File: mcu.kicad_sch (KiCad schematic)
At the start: 7 parts, among them SW1 SW_MEC_5E, U9 ESP32-S3-WROOM-1-N16R8

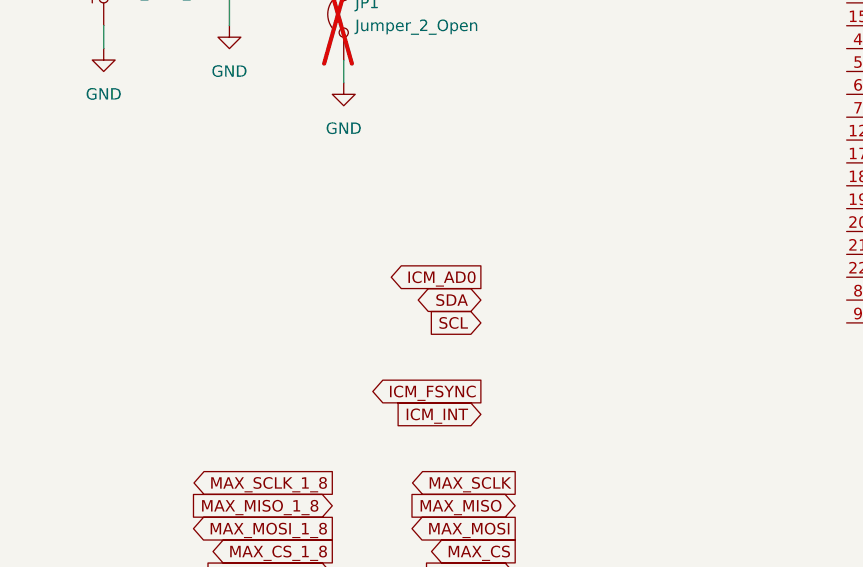
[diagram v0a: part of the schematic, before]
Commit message: Add power rail
Battery charger
3.3V LDO
1.8V LDO
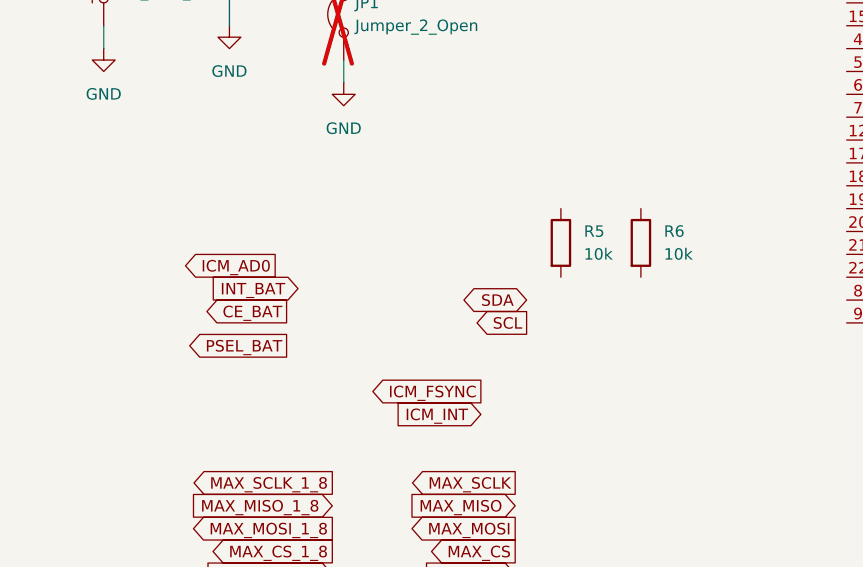
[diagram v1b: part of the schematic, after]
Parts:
- added R5, R6: 10k, symbol Device:R
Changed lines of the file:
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@@
+		)
+	)
+	(global_label "PSEL_BAT"
+		(shape output)
+		(at 77.47 120.65 180)
+		(fields_autoplaced yes)
+		(effects
+			(font
+				(size 1.27 1.27)
+			)
+			(justify right)
+		)
+		(property "Intersheetrefs" "${INTERSHEET_REFS}"
+			(at 65.5344 120.65 0)
+			(effects
+				(font
+					(size 1.27 1.27)
+				)
+				(justify right)
+				(hide yes)
+			)
 		)
 	)
 	(global_label "ICM_AD0"
 		(shape output)
-		(at 99.06 113.03 180)
-		(fields_autoplaced yes)
-		(effects
-			(font
-				(size 1.27 1.27)
-			)
-			(justify right)
-		)
-		(property "Intersheetrefs" "${INTERSHEET_REFS}"
-			(at 88.2129 113.03 0)
+		(at 76.2 111.76 180)
+		(fields_autoplaced yes)
+		(effects
+			(font
+				(size 1.27 1.27)
+			)
+			(justify right)
+		)
+		(property "Intersheetrefs" "${INTERSHEET_REFS}"
+			(at 65.3529 111.76 0)
 			(effects
 				(font
@@
 		)
 	)
+	(global_label "INT_BAT"
+		(shape input)
+		(at 78.74 114.3 180)
+		(fields_autoplaced yes)
+		(effects
+			(font
+				(size 1.27 1.27)
+			)
+			(justify right)
+		)
+		(property "Intersheetrefs" "${INTERSHEET_REFS}"
+			(at 68.5581 114.3 0)
+			(effects
+				(font
+					(size 1.27 1.27)
+				)
+				(justify right)
+				(hide yes)
+			)
+		)
+	)
 	(global_label "D-"
 		(shape bidirectional)
@@
 		)
 	)
+	(global_label "CE_BAT"
+		(shape output)
+		(at 77.47 116.84 180)
+		(fields_autoplaced yes)
+		(effects
+			(font
+				(size 1.27 1.27)
+			)
+			(justify right)
+		)
+		(property "Intersheetrefs" "${INTERSHEET_REFS}"
+			(at 67.772 116.84 0)
+			(effects
+				(font
+					(size 1.27 1.27)
+				)
+				(justify right)
+				(hide yes)
+			)
+		)
+	)
 	(global_label "MAX_INT_1_8"
 		(shape input)
@@
 	)
 	(global_label "SCL"
-		(shape input)
-		(at 99.06 118.11 180)
-		(fields_autoplaced yes)
-		(effects
-			(font
-				(size 1.27 1.27)
-			)
-			(justify right)
-		)
-		(property "Intersheetrefs" "${INTERSHEET_REFS}"
-			(at 92.5672 118.11 0)
+		(shape output)
+		(at 104.14 118.11 180)
+		(fields_autoplaced yes)
+		(effects
+			(font
+				(size 1.27 1.27)
+			)
+			(justify right)
+		)
+		(property "Intersheetrefs" "${INTERSHEET_REFS}"
+			(at 97.6472 118.11 0)
 			(effects
 				(font
@@
 	(global_label "SDA"
 		(shape bidirectional)
-		(at 99.06 115.57 180)
-		(fields_autoplaced yes)
-		(effects
-			(font
-				(size 1.27 1.27)
-			)
-			(justify right)
-		)
-		(property "Intersheetrefs" "${INTERSHEET_REFS}"
-			(at 91.3954 115.57 0)
+		(at 104.14 115.57 180)
+		(fields_autoplaced yes)
+		(effects
+			(font
+				(size 1.27 1.27)
+			)
+			(justify right)
+		)
+		(property "Intersheetrefs" "${INTERSHEET_REFS}"
+			(at 96.4754 115.57 0)
 			(effects
 				(font
@@
 	)
 	(symbol
+		(lib_id "Device:R")
+		(at 116.84 109.22 0)
+		(unit 1)
+		(exclude_from_sim no)
+		(in_bom yes)
+		(on_board yes)
+		(dnp no)
+		(fields_autoplaced yes)
+		(property "Reference" "R6"
+			(at 119.38 107.9499 0)
+			(effects
+				(font
+					(size 1.27 1.27)
+				)
+				(justify left)
+			)
+		)
+		(property "Value" "10k"
+			(at 119.38 110.4899 0)
+			(effects
+				(font
+					(size 1.27 1.27)
+				)
+				(justify left)
+			)
+		)
+		(property "Footprint" ""
+			(at 115.062 109.22 90)
+			(effects
+				(font
+					(size 1.27 1.27)
+				)
+				(hide yes)
+			)
+		)
+		(property "Datasheet" "~"
+			(at 116.84 109.22 0)
+			(effects
+				(font
+					(size 1.27 1.27)
+				)
+				(hide yes)
+			)
+		)
+		(property "Description" "Resistor"
+			(at 116.84 109.22 0)
+			(effects
+				(font
+					(size 1.27 1.27)
+				)
+				(hide yes)
+			)
+		)
+		(pin "2"
+		)
+		(pin "1"
+		)
+		(instances
+			(project "horsesense"
+				(path "/f18e9cf6-8519-4493-9888-bebeac60f18c/4f5da0f7-32d4-4c35-9e09-eaff048f43d5"
+					(reference "R6")
+					(unit 1)
+				)
+			)
+		)
+	)
+	(symbol
 		(lib_id "power:GND")
 		(at 154.94 127 0)
@@
 					(unit 1)
 				)
+			)
+		)
+	)
+	(symbol
+		(lib_id "Device:R")
+		(at 107.95 109.22 0)
+		(unit 1)
+		(exclude_from_sim no)
+		(in_bom yes)
+		(on_board yes)
+		(dnp no)
+		(fields_autoplaced yes)
+		(property "Reference" "R5"
+			(at 110.49 107.9499 0)
+			(effects
+				(font
+					(size 1.27 1.27)
+				)
+				(justify left)
+			)
+		)
+		(property "Value" "10k"
+			(at 110.49 110.4899 0)
+			(effects
+				(font
+					(size 1.27 1.27)
+				)
+				(justify left)
+			)
+		)
+		(property "Footprint" ""
+			(at 106.172 109.22 90)
+			(effects
+				(font
+					(size 1.27 1.27)
+				)
+				(hide yes)
+			)
+		)
+		(property "Datasheet" "~"
+			(at 107.95 109.22 0)
+			(effects
+				(font
+					(size 1.27 1.27)
+				)
+				(hide yes)
+			)
+		)
+		(property "Description" "Resistor"
+			(at 107.95 109.22 0)
+			(effects
+				(font
+					(size 1.27 1.27)
+				)
+				(hide yes)
+			)
+		)
+		(pin "2"
+		)
+		(pin "1"
+		)
+		(instances
+			(project "horsesense"
+				(path "/f18e9cf6-8519-4493-9888-bebeac60f18c/4f5da0f7-32d4-4c35-9e09-eaff048f43d5"
+					(reference "R5")
+					(unit 1)
+				)

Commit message: Routage complet
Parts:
- removed JP1: Jumper_2_Open, Connector_PinHeader_2.54mm:PinHeader_1x02_P2.54mm_Vertical, symbol Jumper:Jumper_2_Open
- added C3, C32: 100n, Capacitor_SMD:C_0805_2012Metric, symbol Device:C
- added J4: Conn_01x04, Connector_PinHeader_1.27mm:PinHeader_1x04_P1.27mm_Vertical, symbol Connector_Generic:Conn_01x04
- added SW2: EVQ-P7A01P, Button_Switch_SMD:SW_SPST_EVQP7A, symbol Switch:SW_Omron_B3FS
- added U2: TXB0304RUT, Package_DFN_QFN:Texas_R-PUQFN-N12, symbol Logic_LevelTranslator:TXB0304RUT
- C24, C25: footprint (none) -> Capacitor_SMD:C_0805_2012Metric
- C37: footprint Capacitor_SMD:C_1206_3216Metric -> Capacitor_SMD:C_0805_2012Metric
- R29: footprint Resistor_SMD:R_1206_3216Metric -> Resistor_SMD:R_0805_2012Metric
- R5, R6: footprint (none) -> Resistor_SMD:R_0805_2012Metric
- SW1: value SW_MEC_5E -> EVQ-P7A01P; footprint Button_Switch_THT:SW_PUSH_6mm_H5mm -> Button_Switch_SMD:SW_SPST_EVQP7A
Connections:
- net +3.3V: now also R5.1, R6.1, C3.1, J4.1 (Pin_1), U2.11 (VCCB)
- net CE_BAT: now also U9.15 (IO3)
- net GND: now also C3.2, C32.2, J4.4 (Pin_4), SW2.1, U2.6 (GND)
- net ICM_AD0: now also U9.39 (IO1)
- net ICM_FSYNC: now also U9.5 (IO5)
- net ICM_INT: now also U9.6 (IO6)
- net INT_BAT: now also U9.38 (IO2)
- net MAX_CS: now also U9.18 (IO10), U2.10 (B1)
- net MAX_CS_1_8: now also U2.2 (A1)
- net MAX_MISO: now also U9.19 (IO11), U2.9 (B2)
- net MAX_MISO_1_8: now also U2.3 (A2)
- net MAX_MOSI: now also U9.21 (IO13), U2.7 (B4)
- net MAX_MOSI_1_8: now also U2.5 (A4)
- net MAX_SCLK: now also U9.20 (IO12), U2.8 (B3)
- net MAX_SCLK_1_8: now also U2.4 (A3)
- net PSEL_BAT: now also U9.4 (IO4)
- net SCL: now also R6.2, U9.9 (IO16)
- net SDA: now also R5.2, U9.8 (IO15)
- net GPS_RX: now reaches U9.10 (IO17)
- net GPS_TX: now reaches U9.11 (IO18)
- net GPS_JAM: now reaches U9.16 (IO46)
- net GPS_FIX: now reaches U9.26 (IO45)
- net at U9.27 (IO0): now also SW2.2
- net GPS_SEL: now reaches U9.31 (IO38)
- net GPS_RST: now reaches U9.32 (IO39)
- net GPS_REQ: now reaches U9.33 (IO40)
- net GPS_PP1: now reaches U9.34 (IO41)
- net GPS_REF: now reaches U9.35 (IO42)
- net at U9.36 (RXD0): now also J4.3 (Pin_3)
- net at U9.37 (TXD0): now also J4.2 (Pin_2)
- net ICM_INT2: now reaches U9.7 (IO7)
- new net +1.8V: C32.1, U2.1 (VCCA), U2.12 (OE)
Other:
- moved on the sheet: C24, C25, C37, R29, R5, R6, SW1, U9

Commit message: Set MPN
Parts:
- C24: JLCPCB Part # (none) -> GRM21BZ71A226ME15L; manf# CC1206KKX7R7BB105 -> GRM21BZ71A226ME15L
- C25, C3, C32: JLCPCB Part # (none) -> CL21B104KBCNNNC; manf# CC1206KKX7R7BB105 -> CL21B104KBCNNNC
- C37: JLCPCB Part # (none) -> CL21B105KAFNFNE; manf# CC1206KKX7R7BB105 -> CL21B105KAFNFNE
- R29: JLCPCB Part # (none) -> RK73H2ATTD1002F; manf# RC1206FR-0710KL -> RK73H2ATTD1002F
- R5, R6: JLCPCB Part # (none) -> RK73H2ATTD1002F; manf# (none) -> RK73H2ATTD1002F
- SW1, SW2: JLCPCB Part # (none) -> EVQ-P7A01P; manf# 1825910-6 -> EVQ-P7A01P
- U2: value TXB0304RUT -> TXB0304RUTR; JLCPCB Part # (none) -> TXB0304RUTR; manf# (none) -> TXB0304RUTR
- U9: JLCPCB Part # (none) -> ESP32-S3-WROOM-1-N16R8
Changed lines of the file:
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@@
 			)
 		)
-		(property "Value" "TXB0304RUT"
+		(property "Value" "TXB0304RUTR"
 			(at 75.8033 162.56 0)
 			(effects
@@
 			)
 		)
+		(property "JLCPCB Part #" "TXB0304RUTR"
+			(at 73.66 142.24 0)
+			(effects
+				(font
+					(size 1.27 1.27)
+				)
+				(hide yes)
+			)
+		)
+		(property "manf#" "TXB0304RUTR"
+			(at 73.66 142.24 0)
+			(effects
+				(font
+					(size 1.27 1.27)
+				)
+				(hide yes)
+			)
+		)
 		(pin "12"
 		)
@@
 			)
 		)
-		(property "manf#" "1825910-6"
+		(property "manf#" "EVQ-P7A01P"
 			(at 44.45 62.23 0)
 			(effects
@@
 			)
 		)
+		(property "JLCPCB Part #" "EVQ-P7A01P"
+			(at 44.45 62.23 90)
+			(effects
+				(font
+					(size 1.27 1.27)
+				)
+				(hide yes)
+			)
+		)
 		(pin "1"
 		)
@@
 			)
 		)
+		(property "JLCPCB Part #" "RK73H2ATTD1002F"
+			(at 76.2 91.44 0)
+			(effects
+				(font
+					(size 1.27 1.27)
+				)
+				(hide yes)
+			)
+		)
+		(property "manf#" "RK73H2ATTD1002F"
+			(at 76.2 91.44 0)
+			(effects
+				(font
+					(size 1.27 1.27)
+				)
+				(hide yes)
+			)
+		)
 		(pin "2"
 		)
@@
 			)
 		)
-		(property "manf#" "RC1206FR-0710KL"
+		(property "manf#" "RK73H2ATTD1002F"
 			(at 31.75 54.61 0)
 			(effects
@@
 			)
 		)
+		(property "JLCPCB Part #" "RK73H2ATTD1002F"
+			(at 31.75 54.61 90)
+			(effects
+				(font
+					(size 1.27 1.27)
+				)
+				(hide yes)
+			)
+		)
 		(pin "1"
 		)
@@
 			)
 		)
+		(property "JLCPCB Part #" "ESP32-S3-WROOM-1-N16R8"
+			(at 142.24 77.47 0)
+			(effects
+				(font
+					(size 1.27 1.27)
+				)
+				(hide yes)
+			)
+		)
 		(pin "38"
 		)
@@
 			)
 		)
+		(property "JLCPCB Part #" ""
+			(at 208.28 54.61 0)
+			(effects
+				(font
+					(size 1.27 1.27)
+				)
+				(hide yes)
+			)
+		)
 		(pin "1"
 		)
@@
 			)
 		)
+		(property "JLCPCB Part #" "RK73H2ATTD1002F"
+			(at 67.31 91.44 0)
+			(effects
+				(font
+					(size 1.27 1.27)
+				)
+				(hide yes)
+			)
+		)
+		(property "manf#" "RK73H2ATTD1002F"
+			(at 67.31 91.44 0)
+			(effects
+				(font
+					(size 1.27 1.27)
+				)
+				(hide yes)
+			)
+		)
 		(pin "2"
 		)
@@
 			)
 		)
-		(property "manf#" " CC1206KKX7R7BB105"
+		(property "manf#" "CL21B104KBCNNNC"
 			(at 92.71 121.92 0)
 			(effects
@@
 			)
 		)
+		(property "JLCPCB Part #" "CL21B104KBCNNNC"
+			(at 92.71 121.92 0)
+			(effects
+				(font
+					(size 1.27 1.27)
+				)
+				(hide yes)
+			)
+		)
 		(pin "2"
 		)
@@
 			)
 		)
-		(property "manf#" " CC1206KKX7R7BB105"
+		(property "manf#" "CL21B104KBCNNNC"
 			(at 170.18 33.02 0)
 			(effects
@@
 			)
 		)
+		(property "JLCPCB Part #" "CL21B104KBCNNNC"
+			(at 170.18 33.02 0)
+			(effects
+				(font
+					(size 1.27 1.27)
+				)
+				(hide yes)
+			)
+		)
 		(pin "2"
 		)
@@
 			)
 		)
-		(property "manf#" " CC1206KKX7R7BB105"
+		(property "manf#" "CL21B104KBCNNNC"
 			(at 40.64 116.84 0)
 			(effects
@@
 			)
 		)
+		(property "JLCPCB Part #" "CL21B104KBCNNNC"
+			(at 40.64 116.84 0)
+			(effects
+				(font
+					(size 1.27 1.27)
+				)
+				(hide yes)
+			)
+		)
 		(pin "2"
 		)
@@
 			)
 		)
-		(property "manf#" " CC1206KKX7R7BB105"
+		(property "manf#" "CL21B105KAFNFNE"
 			(at 58.42 59.69 0)
 			(effects
@@
 			)
 		)
+		(property "JLCPCB Part #" "CL21B105KAFNFNE"
+			(at 58.42 59.69 0)
+			(effects
+				(font
+					(size 1.27 1.27)
+				)
+				(hide yes)
+			)
+		)
 		(pin "2"
 		)
@@
 			)
 		)
-		(property "manf#" "1825910-6"
+		(property "manf#" "EVQ-P7A01P"
 			(at 71.12 66.04 0)
 			(effects
@@
 			)
 		)
+		(property "JLCPCB Part #" "EVQ-P7A01P"
+			(at 71.12 66.04 90)
+			(effects
+				(font
+					(size 1.27 1.27)
+				)
+				(hide yes)
+			)
+		)
 		(pin "1"
 		)
@@
 			)
 		)
-		(property "manf#" " CC1206KKX7R7BB105"
+		(property "manf#" "GRM21BZ71A226ME15L"
 			(at 160.02 33.02 0)
 			(effects
@@
 			(at 160.02 33.02 0)
 			(effects
+				(font
+					(size 1.27 1.27)
+				)
+				(hide yes)
+			)
+		)
+		(property "JLCPCB Part #" "GRM21BZ71A226ME15L"
+			(at 160.02 33.02 0)
+			(effects

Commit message: Change Code for JLC part
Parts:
- C24: JLCPCB Part # GRM21BZ71A226ME15L -> C907991
- C25, C3, C32: JLCPCB Part # CL21B104KBCNNNC -> C1711
- C37: JLCPCB Part # CL21B105KAFNFNE -> C1712
- R29, R5, R6: JLCPCB Part # RK73H2ATTD1002F -> C276215
- SW1, SW2: JLCPCB Part # EVQ-P7A01P -> C79167
- U2: JLCPCB Part # TXB0304RUTR -> C69598
- U9: JLCPCB Part # ESP32-S3-WROOM-1-N16R8 -> C2913202
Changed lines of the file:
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@@
 			)
 		)
-		(property "JLCPCB Part #" "TXB0304RUTR"
+		(property "JLCPCB Part #" "C69598"
 			(at 73.66 142.24 0)
 			(effects
@@
 			)
 		)
-		(property "JLCPCB Part #" "EVQ-P7A01P"
+		(property "JLCPCB Part #" "C79167"
 			(at 44.45 62.23 90)
 			(effects
@@
 			)
 		)
-		(property "JLCPCB Part #" "RK73H2ATTD1002F"
+		(property "JLCPCB Part #" "C276215"
 			(at 76.2 91.44 0)
 			(effects
@@
 			)
 		)
-		(property "JLCPCB Part #" "RK73H2ATTD1002F"
+		(property "JLCPCB Part #" "C276215"
 			(at 31.75 54.61 90)
 			(effects
@@
 			)
 		)
-		(property "JLCPCB Part #" "ESP32-S3-WROOM-1-N16R8"
+		(property "JLCPCB Part #" "C2913202"
 			(at 142.24 77.47 0)
 			(effects
@@
 			)
 		)
-		(property "JLCPCB Part #" "RK73H2ATTD1002F"
+		(property "JLCPCB Part #" "C276215"
 			(at 67.31 91.44 0)
 			(effects
@@
 			)
 		)
-		(property "JLCPCB Part #" "CL21B104KBCNNNC"
+		(property "JLCPCB Part #" "C1711"
 			(at 92.71 121.92 0)
 			(effects
@@
 			)
 		)
-		(property "JLCPCB Part #" "CL21B104KBCNNNC"
+		(property "JLCPCB Part #" "C1711"
 			(at 170.18 33.02 0)
 			(effects
@@
 			)
 		)
-		(property "JLCPCB Part #" "CL21B104KBCNNNC"
+		(property "JLCPCB Part #" "C1711"
 			(at 40.64 116.84 0)
 			(effects
@@
 			)
 		)
-		(property "JLCPCB Part #" "CL21B105KAFNFNE"
+		(property "JLCPCB Part #" "C1712"
 			(at 58.42 59.69 0)
 			(effects
@@
 			)
 		)
-		(property "JLCPCB Part #" "EVQ-P7A01P"
+		(property "JLCPCB Part #" "C79167"
 			(at 71.12 66.04 90)
 			(effects
@@
 			)
 		)
-		(property "JLCPCB Part #" "GRM21BZ71A226ME15L"
+		(property "JLCPCB Part #" "C907991"
 			(at 160.02 33.02 0)
 			(effects
